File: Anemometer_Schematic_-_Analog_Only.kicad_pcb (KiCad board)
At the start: 2 copper layers, 48.8 x 53.1 mm, 48 parts, among them J1 Conn_01x10_Male, Q1 BC857, Q2 BC857, U1 LM324, U2 MAX232

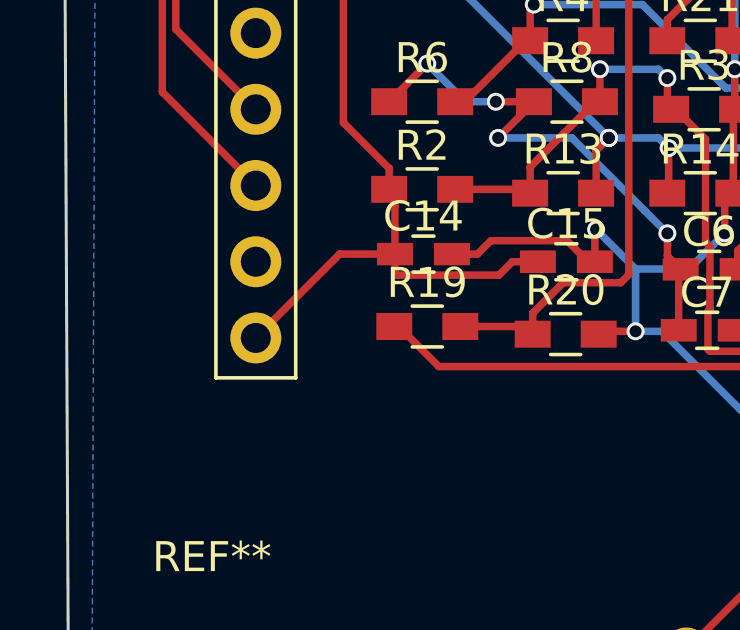
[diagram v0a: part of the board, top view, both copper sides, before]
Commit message: Updated: labeled connector on PCB
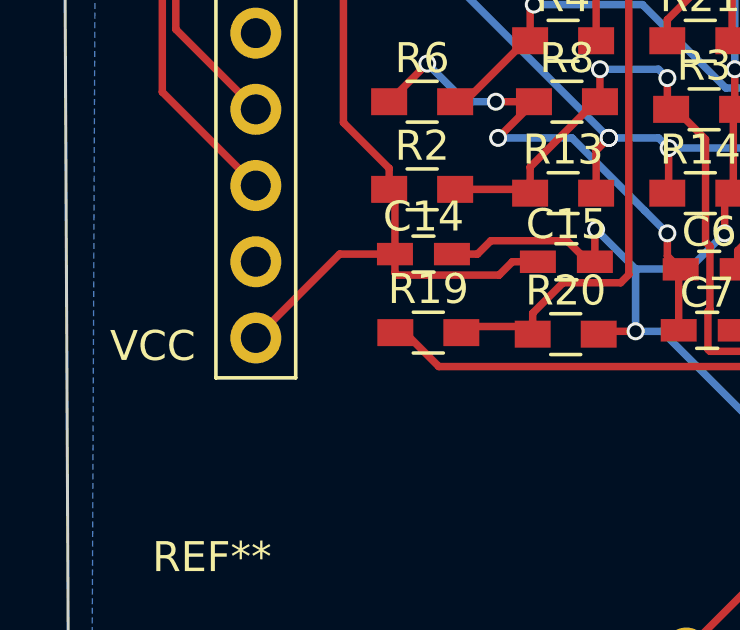
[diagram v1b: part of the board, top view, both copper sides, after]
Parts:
- moved R19 0.21 mm to (100.6, 117.7)
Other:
- board text added: "VCC"
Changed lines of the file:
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@@
     (area 85.135149 78.789 140.602272 135.3944)
     (thickness 1.6)
-    (drawings 4)
+    (drawings 5)
     (tracks 464)
     (zones 0)
@@
   )
   (layers
-    (0 F.Cu signal)
-    (31 B.Cu signal)
-    (32 B.Adhes user)
-    (33 F.Adhes user)
-    (34 B.Paste user)
+    (0 F.Cu signal hide)
+    (31 B.Cu signal hide)
+    (32 B.Adhes user hide)
+    (33 F.Adhes user hide)
+    (34 B.Paste user hide)
     (35 F.Paste user)
-    (36 B.SilkS user)
+    (36 B.SilkS user hide)
     (37 F.SilkS user)
-    (38 B.Mask user)
-    (39 F.Mask user)
-    (40 Dwgs.User user)
+    (38 B.Mask user hide)
+    (39 F.Mask user hide)
+    (40 Dwgs.User user hide)
     (41 Cmts.User user)
     (42 Eco1.User user)
@@
     (44 Edge.Cuts user)
     (45 Margin user)
-    (46 B.CrtYd user)
+    (46 B.CrtYd user hide)
     (47 F.CrtYd user)
     (48 B.Fab user)
-    (49 F.Fab user)
+    (49 F.Fab user hide)
   )
   (setup
@@
   )
   (module Resistors_SMD:R_0603_HandSoldering (layer F.Cu)
-    (at 100.584 117.475)
+    (at 100.61938 117.6782)
     (descr "Resistor SMD 0603, hand soldering")
     (tags "resistor 0603")
@@
     (pad 1 np_thru_hole circle (at 0 0) (size 3.5 3.5) (drill 3.5) (layers *.Cu *.Mask))
   )
+  (gr_text VCC (at 91.43492 118.12778) (layer F.SilkS)
+    (effects (font (size 1 1) (thickness 0.25)))
+  )
   (gr_line (start 88.392 81.28) (end 88.646 134.366) (layer Edge.Cuts) (width 0.1))

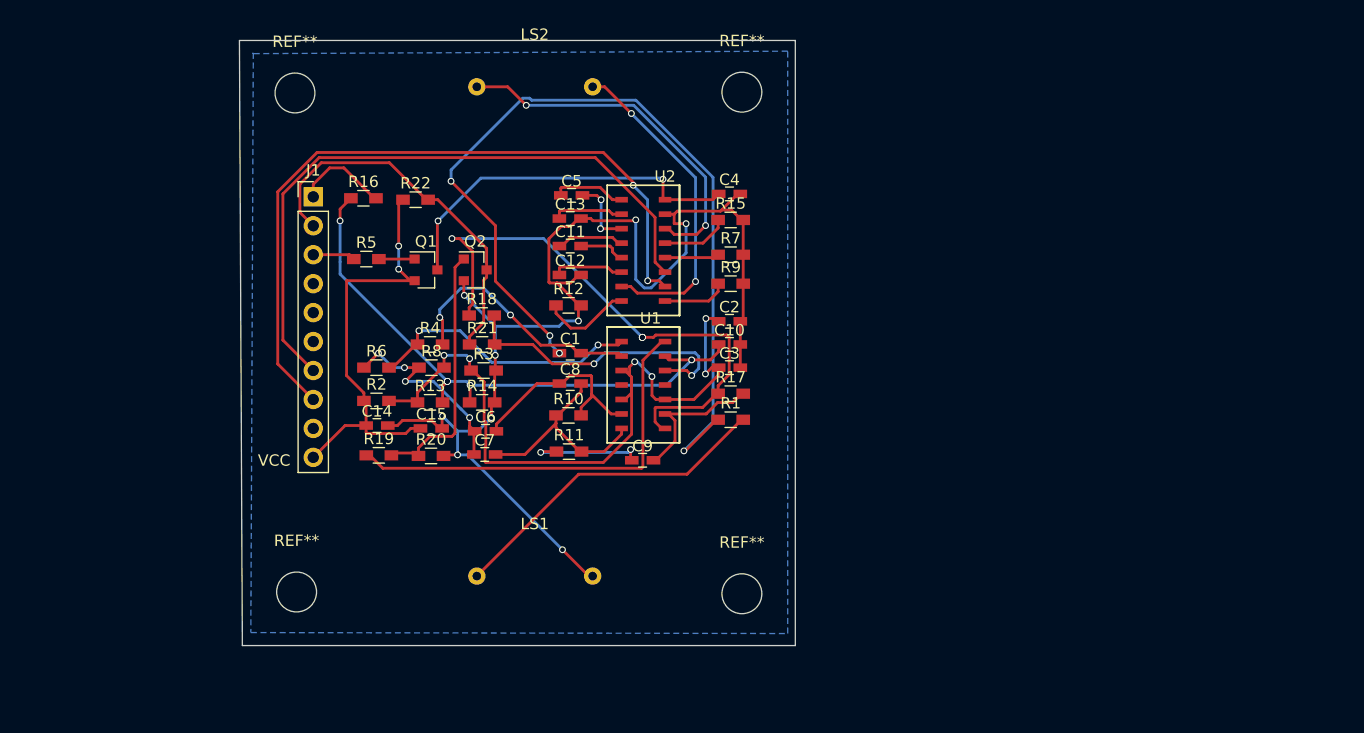
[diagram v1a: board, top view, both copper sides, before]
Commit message: PCB draft 2
Redesigned the PCB to make the layout more optimal. Added VCC and GND connections to U1 in schematic and PCB.
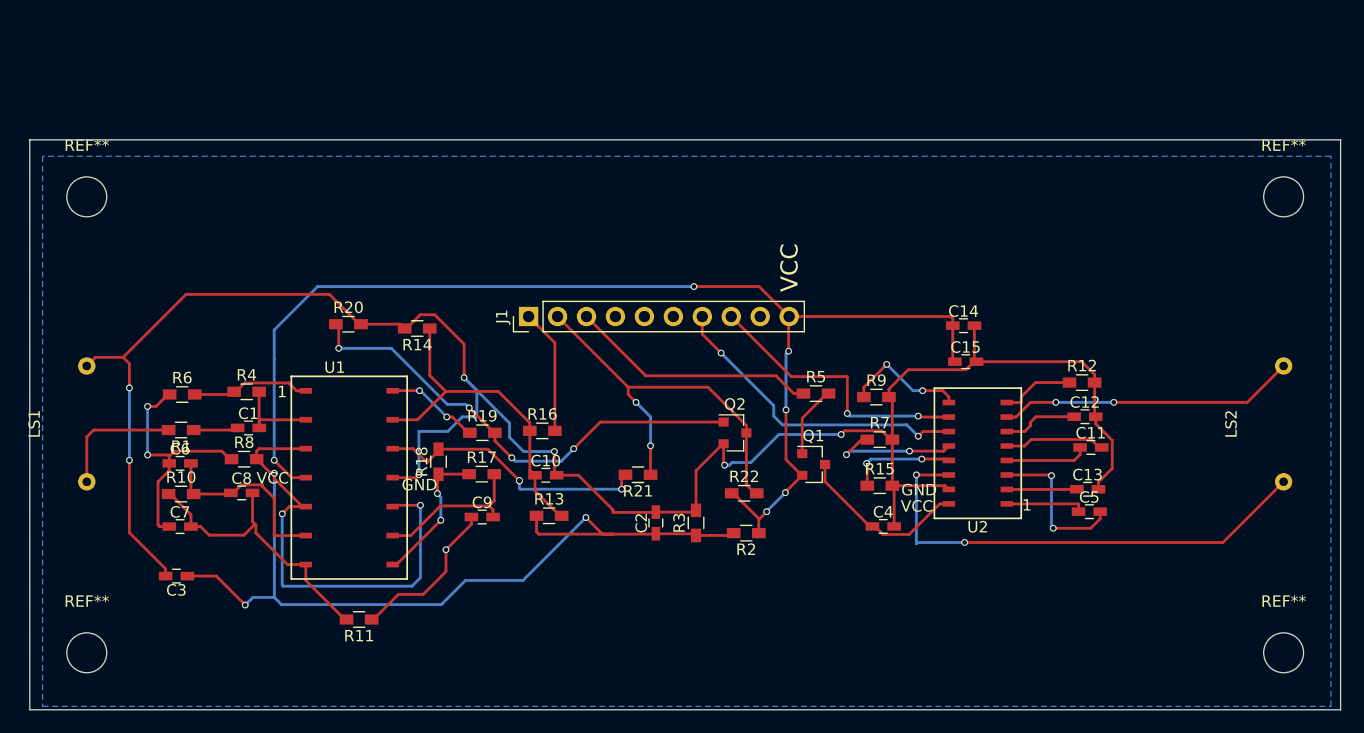
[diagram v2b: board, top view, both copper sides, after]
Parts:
- removed the REF** at (93.3, 85.9)
- removed the REF** at (132.5, 85.8)
- removed the REF** at (93.4, 129.7)
- removed the REF** at (132.5, 129.8)
- added REF**: MountingHole_3.5mm, Mounting_Holes:MountingHole_3.5mm, F.Cu at (75.0, 95.0)
- added REF**: MountingHole_3.5mm, Mounting_Holes:MountingHole_3.5mm, F.Cu at (75.0, 135.0)
- added REF**: MountingHole_3.5mm, Mounting_Holes:MountingHole_3.5mm, F.Cu at (180.0, 135.0)
- added REF**: MountingHole_3.5mm, Mounting_Holes:MountingHole_3.5mm, F.Cu at (180.0, 95.0)
- moved LS2 69.8 mm to (174.9, 114.9), turned to 90 degrees
- moved C5 53.2 mm to (163.0, 122.6)
- moved C14 52.2 mm to (151.9, 106.3)
- moved C3 51.8 mm to (82.9, 128.3), turned to 180 degrees
- moved C13 51.2 mm to (162.8, 120.7)
- moved C11 49.0 mm to (163.1, 117.0)
- moved R1 48.2 mm to (83.3, 115.5), turned to 180 degrees
- moved C15 47.3 mm to (152.1, 109.5)
- moved C12 46.8 mm to (162.6, 114.3)
- moved R12 45.6 mm to (162.3, 111.3)
- moved LS1 45.1 mm to (69.9, 114.9), turned to 90 degrees
- moved R5 41.2 mm to (139.0, 112.3)
- moved U2 40.4 mm to (150.6, 124.5), turned to 180 degrees
- moved R22 38.7 mm to (132.7, 121.0)
- moved Q1 38.1 mm to (138.8, 118.5)
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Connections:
- U1 pad 11: Net-(U1-Pad11) -> GND
- U1 pad 4: Net-(U1-Pad4) -> VCC
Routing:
- net Net-(C1-Pad1): track 77.7 -> 3.93 mm, vias 4 -> 0
- net GND: track 110.2 -> 181.6 mm, vias 9 -> 7
- net VCC: track 38.9 -> 105.6 mm, vias 2 -> 6
- net Net-(C2-Pad1): track 62.3 -> 114.7 mm, vias 6 -> 5
- net Net-(J1-Pad8): track 64.1 -> 24.6 mm
- net Net-(R17-Pad1): track 49.8 -> 12.7 mm, vias 4 -> 2
- net Net-(J1-Pad7): track 57.9 -> 27.6 mm, vias 0 -> 2
- net Net-(R19-Pad1): track 36.9 -> 8.41 mm, vias 0 -> 2
- net Net-(C10-Pad1): track 52.2 -> 29.8 mm, vias 5 -> 0
- net Net-(Q2-Pad1): track 22.6 -> 42.3 mm, vias 0 -> 4
- net Net-(J1-Pad3): track 3.71 -> 21.8 mm
- net Net-(LS1-Pad1): track 29.0 -> 11.4 mm
- net Net-(C4-Pad1): track 32.4 -> 15.4 mm, vias 2 -> 0
- net Net-(C1-Pad2): track 22.4 -> 7.92 mm, vias 2 -> 0
- net Net-(R4-Pad1): track 24.3 -> 10.5 mm, vias 2 -> 0
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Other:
- board size 48.8 x 53.1 mm -> 115 x 50 mm
- board text added: "1"
- board text added: "GND"
